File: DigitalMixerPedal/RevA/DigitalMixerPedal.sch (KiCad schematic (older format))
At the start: 14 parts, among them J1 MonoJack2Switch, J2 MonoJack2Switch, J3 MonoJack2Switch, J4 MonoJack2Switch, J5 Barrel_Jack, J6 MonoJack2Switch

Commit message: hw update
RevA layout completed (draft)
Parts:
- removed R29, R31, R32, R33: 100R, Resistor_SMD:R_0805_2012Metric_Pad1.15x1.40mm_HandSolder, symbol Device:R
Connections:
- net GNDS: now also J1.2 (TIP_NC), J2.2 (TIP_NC), J3.2 (TIP_NC), J4.2 (TIP_NC)
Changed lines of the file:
@@
 	9850 3425 9850 3900
-Wire Wire Line
-	1550 1025 1575 1025
 Wire Wire Line
 	1950 1025 1950 1125
@@
 	1550 2700 1950 2700
 Connection ~ 1950 2700
-Wire Wire Line
-	1550 3975 1575 3975
 Wire Wire Line
 	1950 3975 1950 4075
@@
 Wire Wire Line
 	1950 2700 1950 2900
-$Comp
-L Device:R R?
-U 1 1 5F626ED9
-P 1725 1025
-AR Path="/5F3F1F31/5F626ED9" Ref="R?"  Part="1"
-AR Path="/5F512144/5F626ED9" Ref="R?"  Part="1"
-AR Path="/5F515E89/5F626ED9" Ref="R?"  Part="1"
-AR Path="/5F519B24/5F626ED9" Ref="R?"  Part="1"
-AR Path="/5F41651F/5F626ED9" Ref="R?"  Part="1"
-AR Path="/5F626ED9" Ref="R31"  Part="1"
-F 0 "R31" V 1725 1475 50  0000 C CNN
-F 1 "100R" V 1800 1475 50  0000 C CNN
-F 2 "Resistor_SMD:R_0805_2012Metric_Pad1.15x1.40mm_HandSolder" V 1655 1025 50  0001 C CNN
-F 3 "~" H 1725 1025 50  0001 C CNN
-	1    1725 1025
-	0    1    1    0
-$EndComp
-Wire Wire Line
-	1875 1025 1950 1025
-Wire Wire Line
-	1550 2500 1575 2500
-$Comp
-L Device:R R?
-U 1 1 5F627E07
-P 1725 2500
-AR Path="/5F3F1F31/5F627E07" Ref="R?"  Part="1"
-AR Path="/5F512144/5F627E07" Ref="R?"  Part="1"
-AR Path="/5F515E89/5F627E07" Ref="R?"  Part="1"
-AR Path="/5F519B24/5F627E07" Ref="R?"  Part="1"
-AR Path="/5F41651F/5F627E07" Ref="R?"  Part="1"
-AR Path="/5F627E07" Ref="R32"  Part="1"
-F 0 "R32" V 1725 2925 50  0000 C CNN
-F 1 "100R" V 1800 2925 50  0000 C CNN
-F 2 "Resistor_SMD:R_0805_2012Metric_Pad1.15x1.40mm_HandSolder" V 1655 2500 50  0001 C CNN
-F 3 "~" H 1725 2500 50  0001 C CNN
-	1    1725 2500
-	0    1    1    0
-$EndComp
-Wire Wire Line
-	1875 2500 1950 2500
-$Comp
-L Device:R R?
-U 1 1 5F62815E
-P 1725 3975
-AR Path="/5F3F1F31/5F62815E" Ref="R?"  Part="1"
-AR Path="/5F512144/5F62815E" Ref="R?"  Part="1"
-AR Path="/5F515E89/5F62815E" Ref="R?"  Part="1"
-AR Path="/5F519B24/5F62815E" Ref="R?"  Part="1"
-AR Path="/5F41651F/5F62815E" Ref="R?"  Part="1"
-AR Path="/5F62815E" Ref="R33"  Part="1"
-F 0 "R33" V 1725 4425 50  0000 C CNN
-F 1 "100R" V 1800 4425 50  0000 C CNN
-F 2 "Resistor_SMD:R_0805_2012Metric_Pad1.15x1.40mm_HandSolder" V 1655 3975 50  0001 C CNN
-F 3 "~" H 1725 3975 50  0001 C CNN
-	1    1725 3975
-	0    1    1    0
-$EndComp
-Wire Wire Line
-	1875 3975 1950 3975
-$Comp
-L Device:R R?
-U 1 1 5F628BFA
-P 1700 5500
-AR Path="/5F3F1F31/5F628BFA" Ref="R?"  Part="1"
-AR Path="/5F512144/5F628BFA" Ref="R?"  Part="1"
-AR Path="/5F515E89/5F628BFA" Ref="R?"  Part="1"
-AR Path="/5F519B24/5F628BFA" Ref="R?"  Part="1"
-AR Path="/5F41651F/5F628BFA" Ref="R?"  Part="1"
-AR Path="/5F628BFA" Ref="R29"  Part="1"
-F 0 "R29" V 1700 5950 50  0000 C CNN
-F 1 "100R" V 1775 5950 50  0000 C CNN
-F 2 "Resistor_SMD:R_0805_2012Metric_Pad1.15x1.40mm_HandSolder" V 1630 5500 50  0001 C CNN
-F 3 "~" H 1700 5500 50  0001 C CNN
-	1    1700 5500
-	0    1    1    0
-$EndComp
-Wire Wire Line
-	1850 5500 1950 5500
 $Sheet
 S 3525 6900 1450 500
@@
 Wire Wire Line
 	5275 7150 5575 7150
+Wire Wire Line
+	1550 1025 1950 1025
+Wire Wire Line
+	1550 2500 1950 2500
+Wire Wire Line
+	1550 3975 1950 3975
+Wire Wire Line
+	1550 5500 1950 5500
 $EndSCHEMATC

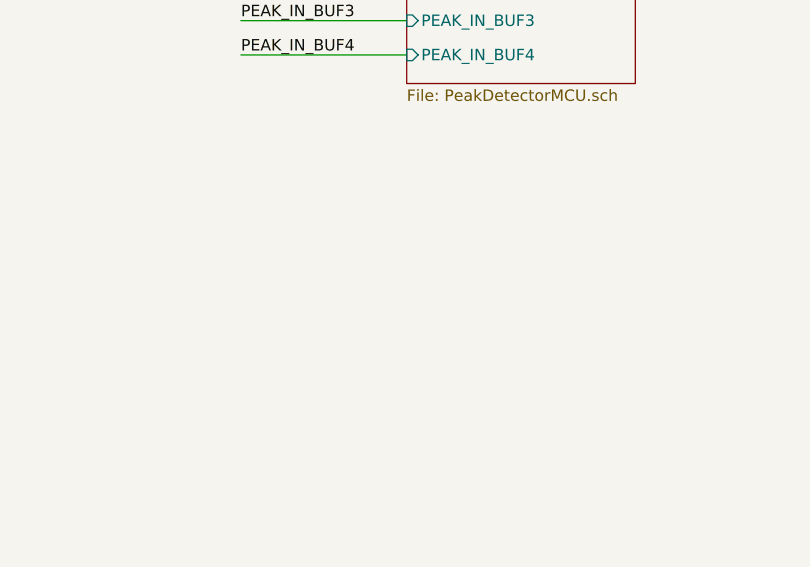
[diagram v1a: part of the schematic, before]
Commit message: updated hw
- added testpoints
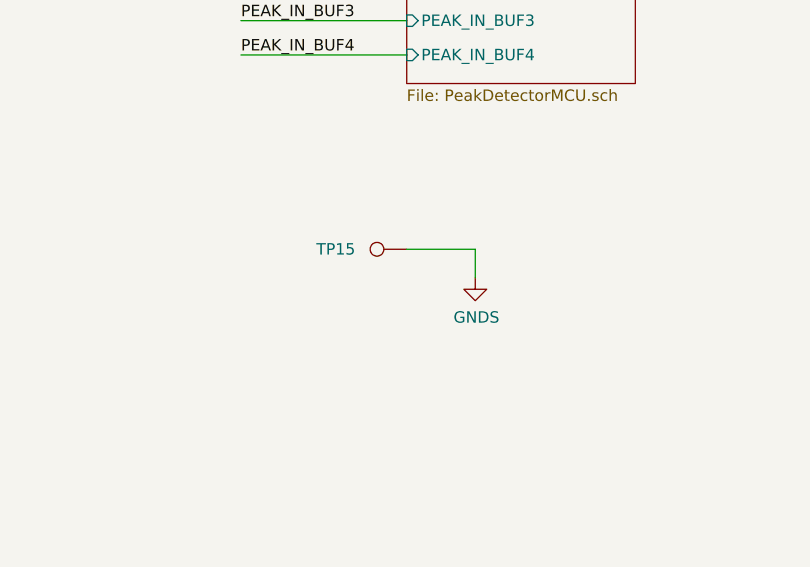
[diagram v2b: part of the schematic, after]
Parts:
- added TP15: TestPoint, TestPoint:TestPoint_Pad_D1.0mm, symbol Connector:TestPoint
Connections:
- net GNDS: now also TP15.1
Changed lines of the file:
@@
 Wire Wire Line
 	1550 5500 1950 5500
+$Comp
+L Connector:TestPoint TP?
+U 1 1 5F746E1D
+P 8875 6025
+AR Path="/5F6E135D/5F746E1D" Ref="TP?"  Part="1"
+AR Path="/5F6E91E5/5F746E1D" Ref="TP?"  Part="1"
+AR Path="/5F6EDB29/5F746E1D" Ref="TP?"  Part="1"
+AR Path="/5F6F225F/5F746E1D" Ref="TP?"  Part="1"
+AR Path="/5F74C2DC/5F746E1D" Ref="TP?"  Part="1"
+AR Path="/5F7234CD/5F746E1D" Ref="TP?"  Part="1"
+AR Path="/5F746E1D" Ref="TP15"  Part="1"
+F 0 "TP15" V 8875 6250 50  0000 L CNN
+F 1 "TestPoint" H 8933 6052 50  0001 L CNN
+F 2 "TestPoint:TestPoint_Pad_D1.0mm" H 9075 6025 50  0001 C CNN
+F 3 "~" H 9075 6025 50  0001 C CNN
+	1    8875 6025
+	0    -1   -1   0
+$EndComp
+Wire Wire Line
+	8875 6025 9175 6025
+Wire Wire Line
+	9175 6025 9175 6150
+$Comp
+L power:GNDS #PWR061
+U 1 1 5F74C4A7
+P 9175 6150
+F 0 "#PWR061" H 9175 5900 50  0001 C CNN
+F 1 "GNDS" H 9180 5977 50  0000 C CNN
+F 2 "" H 9175 6150 50  0001 C CNN
+F 3 "" H 9175 6150 50  0001 C CNN
+	1    9175 6150
+	1    0    0    -1
+$EndComp
 $EndSCHEMATC
